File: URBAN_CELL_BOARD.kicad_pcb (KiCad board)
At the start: 2 copper layers, 162 x 181.6 mm, 20 parts, among them J1 Conn_02x09_Odd_Even, J2 Conn_01x01_Socket, J3 Conn_01x01_Socket, J4 Conn_01x01_Socket, J5 Conn_01x01_Socket

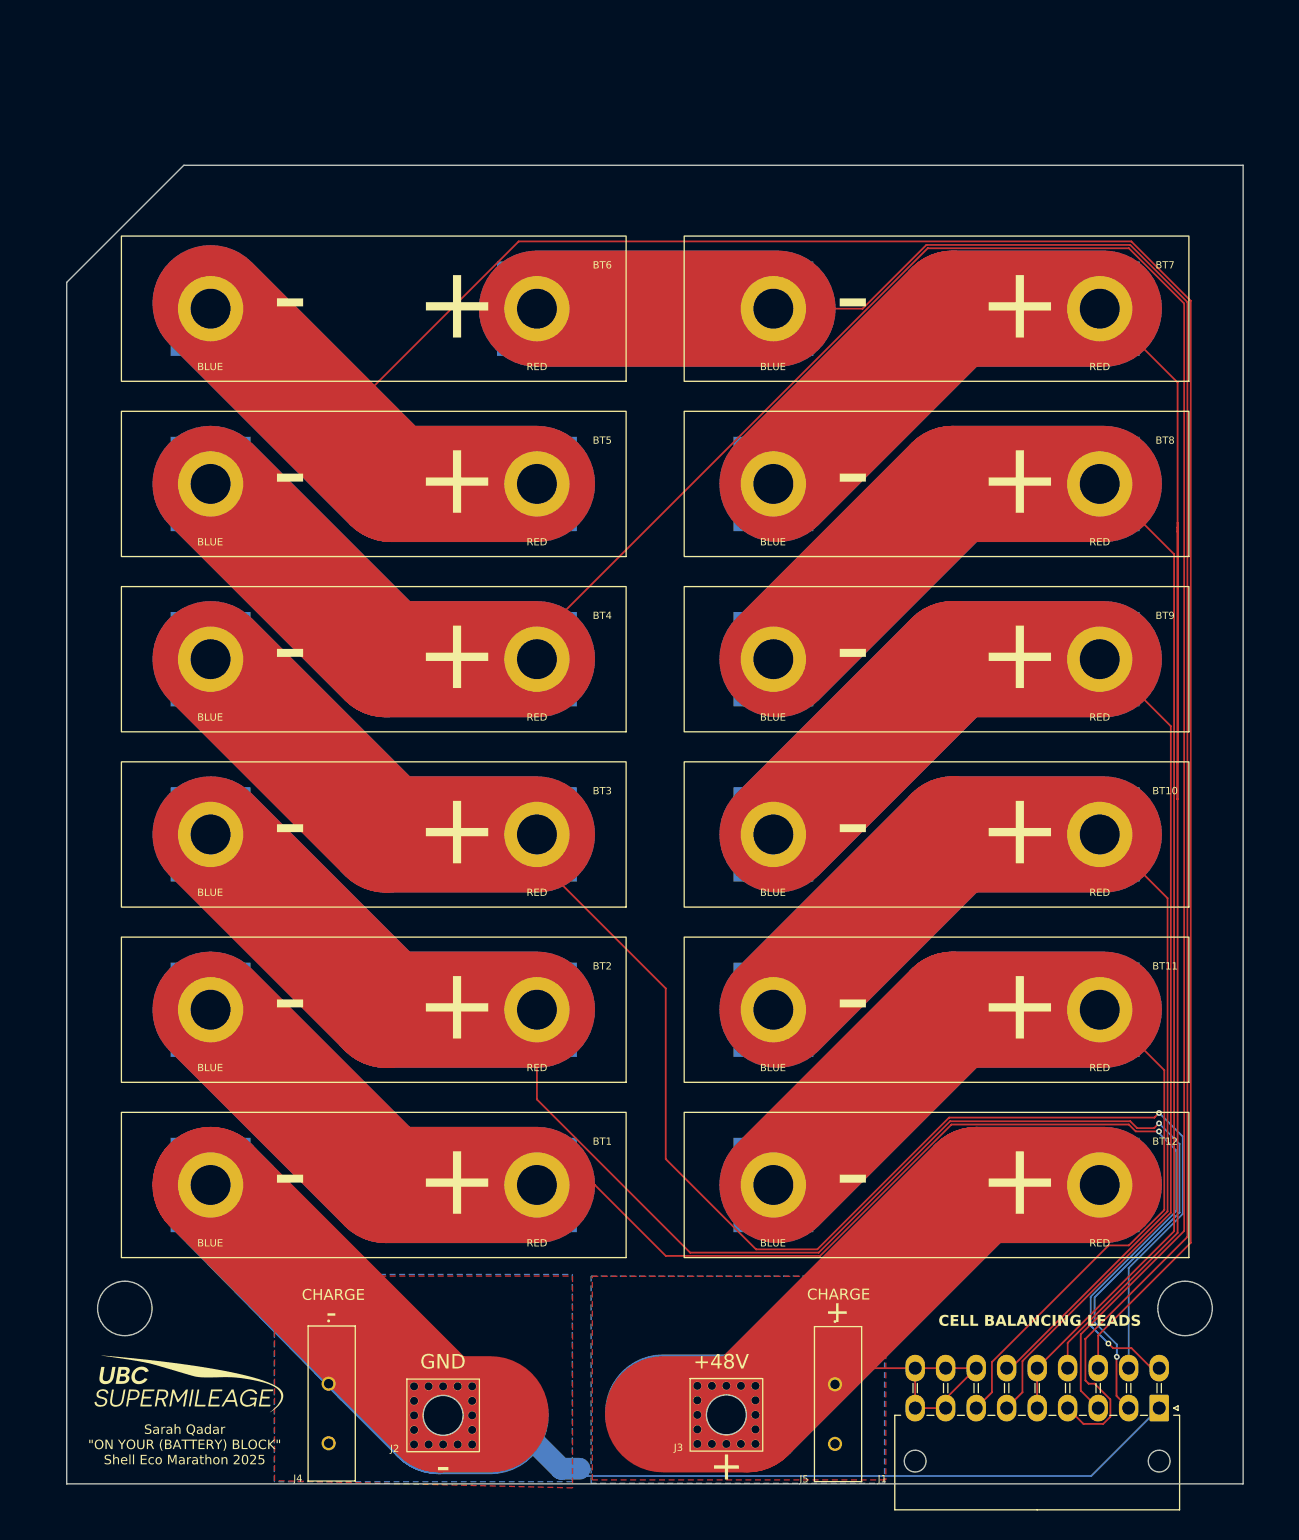
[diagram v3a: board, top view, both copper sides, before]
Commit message: new PCB layout with new cell footprint
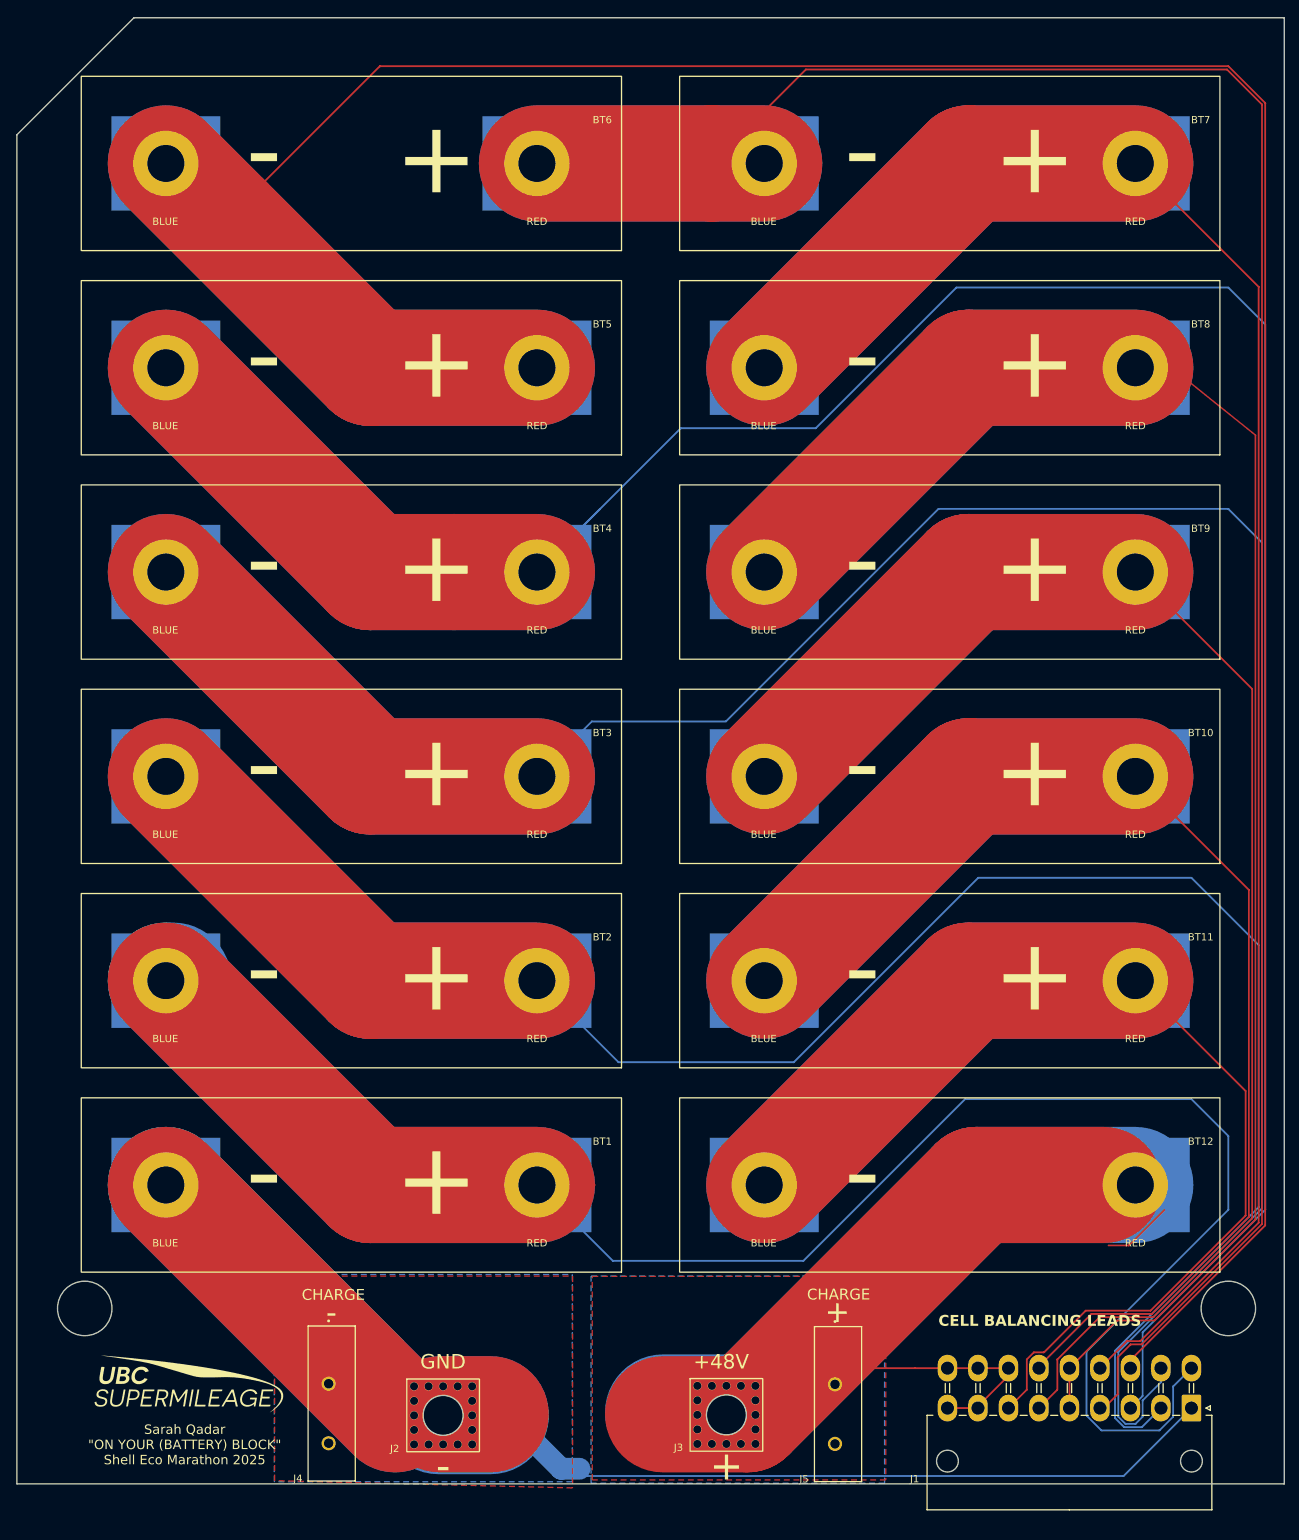
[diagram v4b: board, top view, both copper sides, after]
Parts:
- BT1, BT10, BT11, BT12, BT2, BT3, BT4, BT5, BT6, BT7, BT8, BT9: footprint Battery:Energus Li1x4pVTC6T -> URBAN_CELL_CUSTOM_footprints:Enepaq Molicel P50B 21700
- moved BT7 20.6 mm to (231.0, 99.8)
- moved BT6 20.0 mm to (148.6, 99.8)
- moved BT8 16.7 mm to (231.0, 127.9)
- moved BT5 16.0 mm to (148.6, 127.9)
- moved BT9 13.0 mm to (231.0, 156.0)
- moved BT4 12.0 mm to (148.6, 156.0)
- moved BT10 9.38 mm to (231.0, 184.2)
- moved BT3 8.00 mm to (148.6, 184.2)
- moved BT11 6.33 mm to (231.0, 212.3)
- moved H2 5.96 mm to (243.8, 257.4)
- moved H1 5.52 mm to (86.4, 257.4)
- moved BT12 4.90 mm to (231.0, 240.4)
- moved J1 4.44 mm to (238.8, 271.1)
- moved BT2 4.00 mm to (148.6, 212.3)
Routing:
- net cell3+: track 282.4 -> 391.6 mm, vias 1 -> 0
- net cell5+: track 395.1 -> 469.7 mm
- net cell1+: track 252.0 -> 314.1 mm, vias 2 -> 0
- net cell2+: track 272.0 -> 325.2 mm, vias 2 -> 0
- net GND: track 206.4 -> 259.2 mm
- net cell6+: track 298.0 -> 335.7 mm
- net cell9+: track 226.2 -> 263.8 mm
- net cell10+: track 196.5 -> 230.4 mm
- net cell4+: track 386.2 -> 418.2 mm
- net cell11+: track 180.5 -> 210.2 mm
- net cell8+: track 249.0 -> 274.5 mm
- net +48V: track 193.7 -> 208.4 mm
- net cell7+: track 305.0 -> 308.6 mm
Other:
- board size 162 x 181.6 mm -> 174.5 x 201.9 mm

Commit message: new PCB layout with new cell footprint
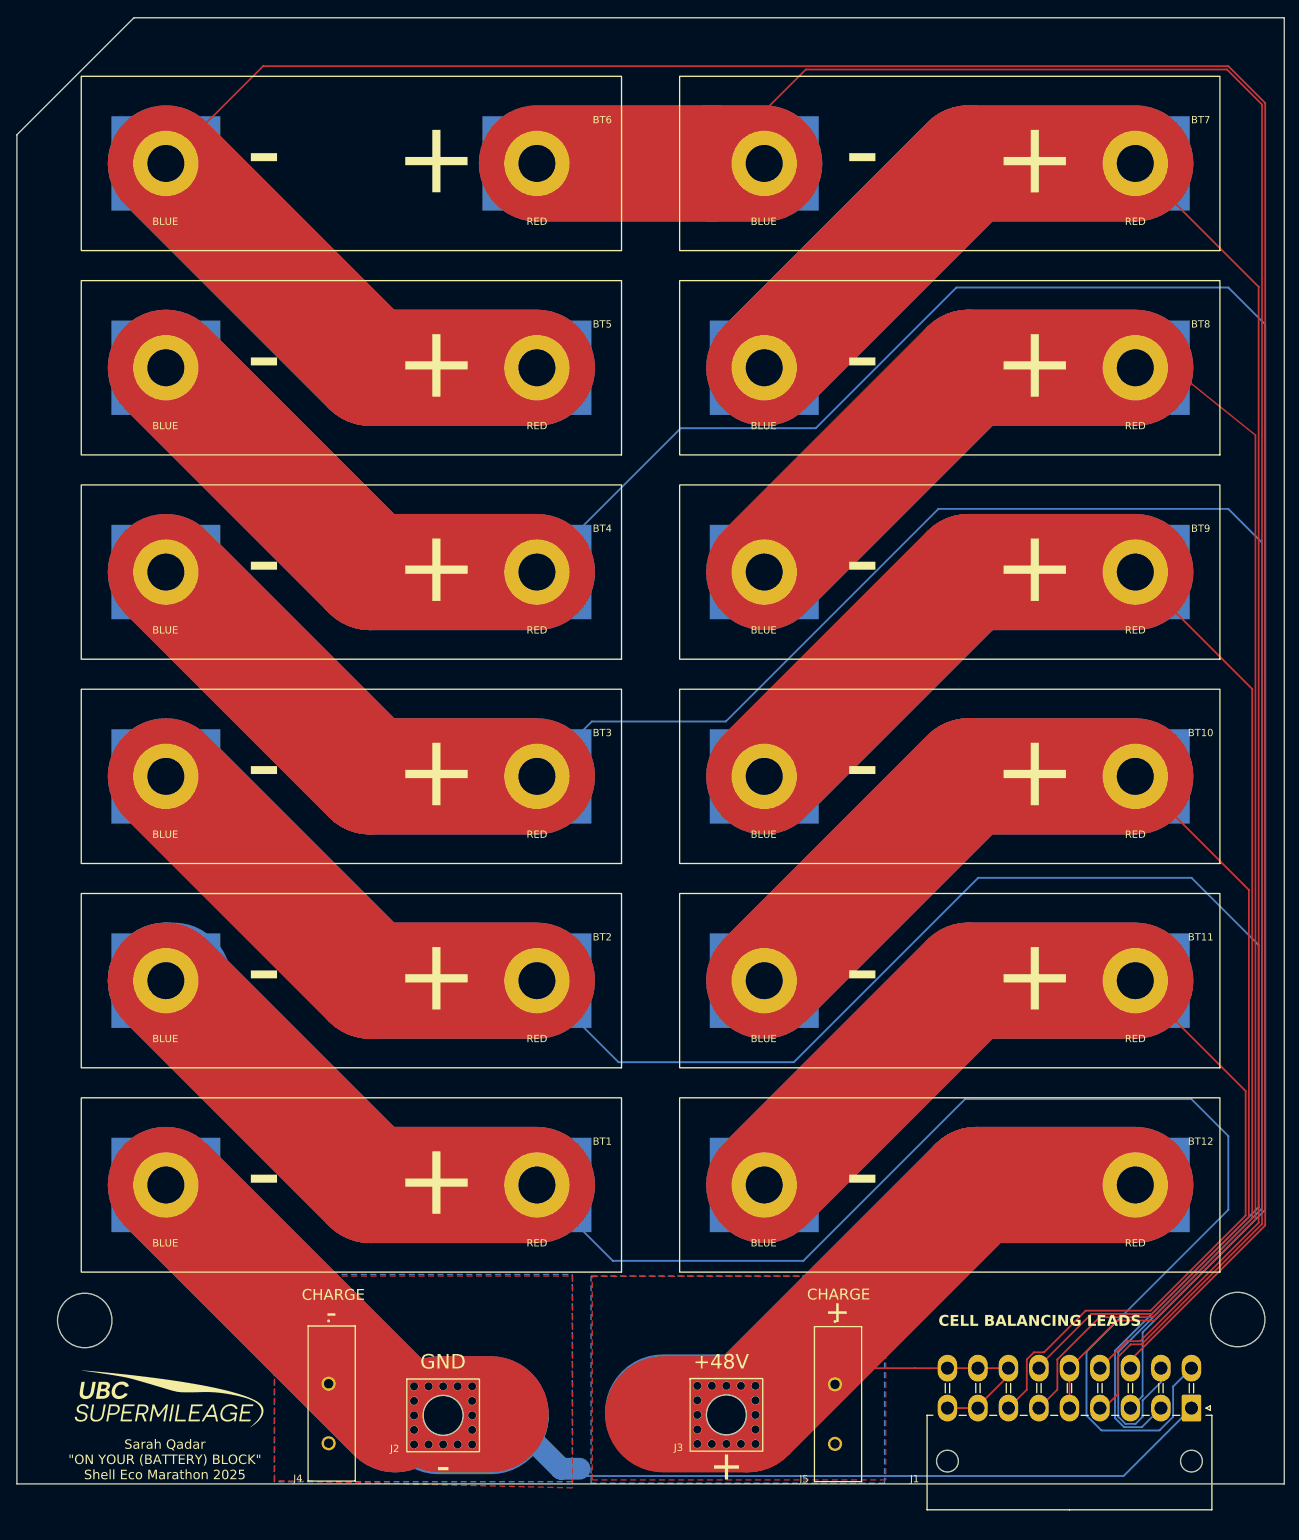
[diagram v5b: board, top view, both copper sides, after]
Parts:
- moved G*** 3.41 mm to (97.8, 270.6)
- moved H2 2.00 mm to (245.1, 259.0)
- moved H1 1.66 mm to (86.4, 259.1)
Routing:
- net GND: track 259.2 -> 221.2 mm
- net cell4+: track 418.2 -> 401.0 mm
- net cell1+: track 314.1 -> 306.1 mm
- net +48V: track 208.4 -> 203.1 mm
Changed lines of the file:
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@@
 	(footprint "LOGO"
 		(layer "F.Cu")
-		(at 100.51 268.56)
+		(at 97.788475 270.613112)
 		(property "Reference" "G***"
 			(at 0 0 0)
@@
 	(footprint "MountingHole:MountingHole_8.4mm_M8"
 		(layer "F.Cu")
-		(at 243.84 257.421)
+		(at 245.130768 258.950923)
 		(descr "Mounting Hole 8.4mm, no annular, M8")
 		(tags "mounting hole 8.4mm no annular m8")
@@
 	(footprint "MountingHole:MountingHole_8.4mm_M8"
 		(layer "F.Cu")
-		(at 86.36 257.421)
+		(at 86.36 259.08)
 		(descr "Mounting Hole 8.4mm, no annular, M8")
 		(tags "mounting hole 8.4mm no annular m8")
@@
 	)
 	(gr_text "Sarah Qadar\n{dblquote}ON YOUR (BATTERY) BLOCK{dblquote}\nShell Eco Marathon 2025"
-		(at 100.12 276.19 0)
+		(at 97.398475 278.243112 0)
 		(layer "F.SilkS")
 		(effects
@@
 	)
 	(segment
-		(start 156.601 240.421)
-		(end 148.629 240.421)
-		(width 0.25)
-		(layer "F.Cu")
-		(net 1)
-	)
-	(segment
 		(start 125.663 240.421)
 		(end 97.529 212.287)
@@
 	)
 	(segment
-		(start 97.529 240.421)
-		(end 124.359023 267.251023)
-		(width 16)
-		(layer "B.Cu")
-		(net 2)
-	)
-	(segment
 		(start 154.5 279.5)
 		(end 151.96 279.5)
@@
 	)
 	(segment
-		(start 243.84 86.36)
-		(end 127 86.36)
-		(width 0.25)
-		(layer "F.Cu")
-		(net 4)
-	)
-	(segment
 		(start 230.36 265.645)
 		(end 230.36 264.545)
@@
 	)
 	(segment
-		(start 105.569 102.711)
-		(end 105.569 107.791)
+		(start 230.36 264.545)
+		(end 248.92 245.985)
 		(width 0.25)
 		(layer "F.Cu")
@@
 	)
 	(segment
-		(start 248.92 245.985)
-		(end 248.92 243.84)
+		(start 243.84 86.36)
+		(end 110.92 86.36)
 		(width 0.25)
 		(layer "F.Cu")
@@
 	)
 	(segment
-		(start 248.92 91.44)
-		(end 243.84 86.36)
+		(start 248.92 245.985)
+		(end 248.92 91.44)
 		(width 0.25)
 		(layer "F.Cu")
@@
 	)
 	(segment
-		(start 105.569 107.791)
+		(start 110.92 86.36)
 		(end 97.529 99.751)
-		(width 16)
-		(layer "F.Cu")
-		(net 4)
-	)
-	(segment
-		(start 127 86.36)
-		(end 105.569 107.791)
 		(width 0.25)
 		(layer "F.Cu")
@@
 	)
 	(segment
-		(start 125.663 127.885)
-		(end 105.569 107.791)
-		(width 16)
-		(layer "F.Cu")
-		(net 4)
-	)
-	(segment
-		(start 230.36 264.545)
-		(end 248.92 245.985)
+		(start 248.92 91.44)
+		(end 243.84 86.36)
 		(width 0.25)
 		(layer "F.Cu")
@@
 	)
 	(segment
-		(start 248.92 243.84)
-		(end 248.92 91.44)
-		(width 0.25)
+		(start 97.529 99.751)
+		(end 125.663 127.885)
+		(width 16)
 		(layer "F.Cu")
 		(net 4)
@@
 	)
 	(segment
-		(start 137.16 156.019)
-		(end 137.16 151.127328)
-		(width 0.25)
-		(layer "F.Cu")
-		(net 5)
-	)
-	(segment
 		(start 97.529 127.885)
 		(end 125.663 156.019)
@@
 	(segment
 		(start 125.663 156.019)
-		(end 137.16 156.019)
-		(width 16)
-		(layer "F.Cu")
-		(net 5)
-	)
-	(segment
-		(start 137.16 156.019)
 		(end 148.629 156.019)
 		(width 16)
@@
 	)
 	(segment
-		(start 157.328 147.32)
-		(end 148.629 156.019)
-		(width 0.25)
-		(layer "B.Cu")
-		(net 5)
-	)
-	(segment
 		(start 206.389344 116.84)
 		(end 243.84 116.84)
@@
 	)
 	(segment
-		(start 148.629 156.019)
-		(end 168.433328 136.214672)
+		(start 168.433328 136.214672)
+		(end 148.629 156.019)
 		(width 0.25)
 		(layer "B.Cu")
@@
 	)
 	(segment
-		(start 209.159 240.421)
-		(end 226.695 240.421)
-		(width 16)
-		(layer "F.Cu")
-		(net 8)
-	)
-	(segment
 		(start 191.795 265.645)
 		(end 188 269.44)
@@
 	)
 	(segment
-		(start 230.143328 248.746)
-		(end 235.02 243.869328)
-		(width 0.25)
+		(start 209.159 240.421)
+		(end 231.029 240.421)
+		(width 16)
 		(layer "F.Cu")
 		(net 8)
@@
 		(layer "F.Cu")
 		(net 8)
-	)
-	(segment
-		(start 227.345192 248.746)
-		(end 230.143328 248.746)
-		(width 0.25)
-		(layer "F.Cu")
-		(net 8)

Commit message: updated footprint again with traces
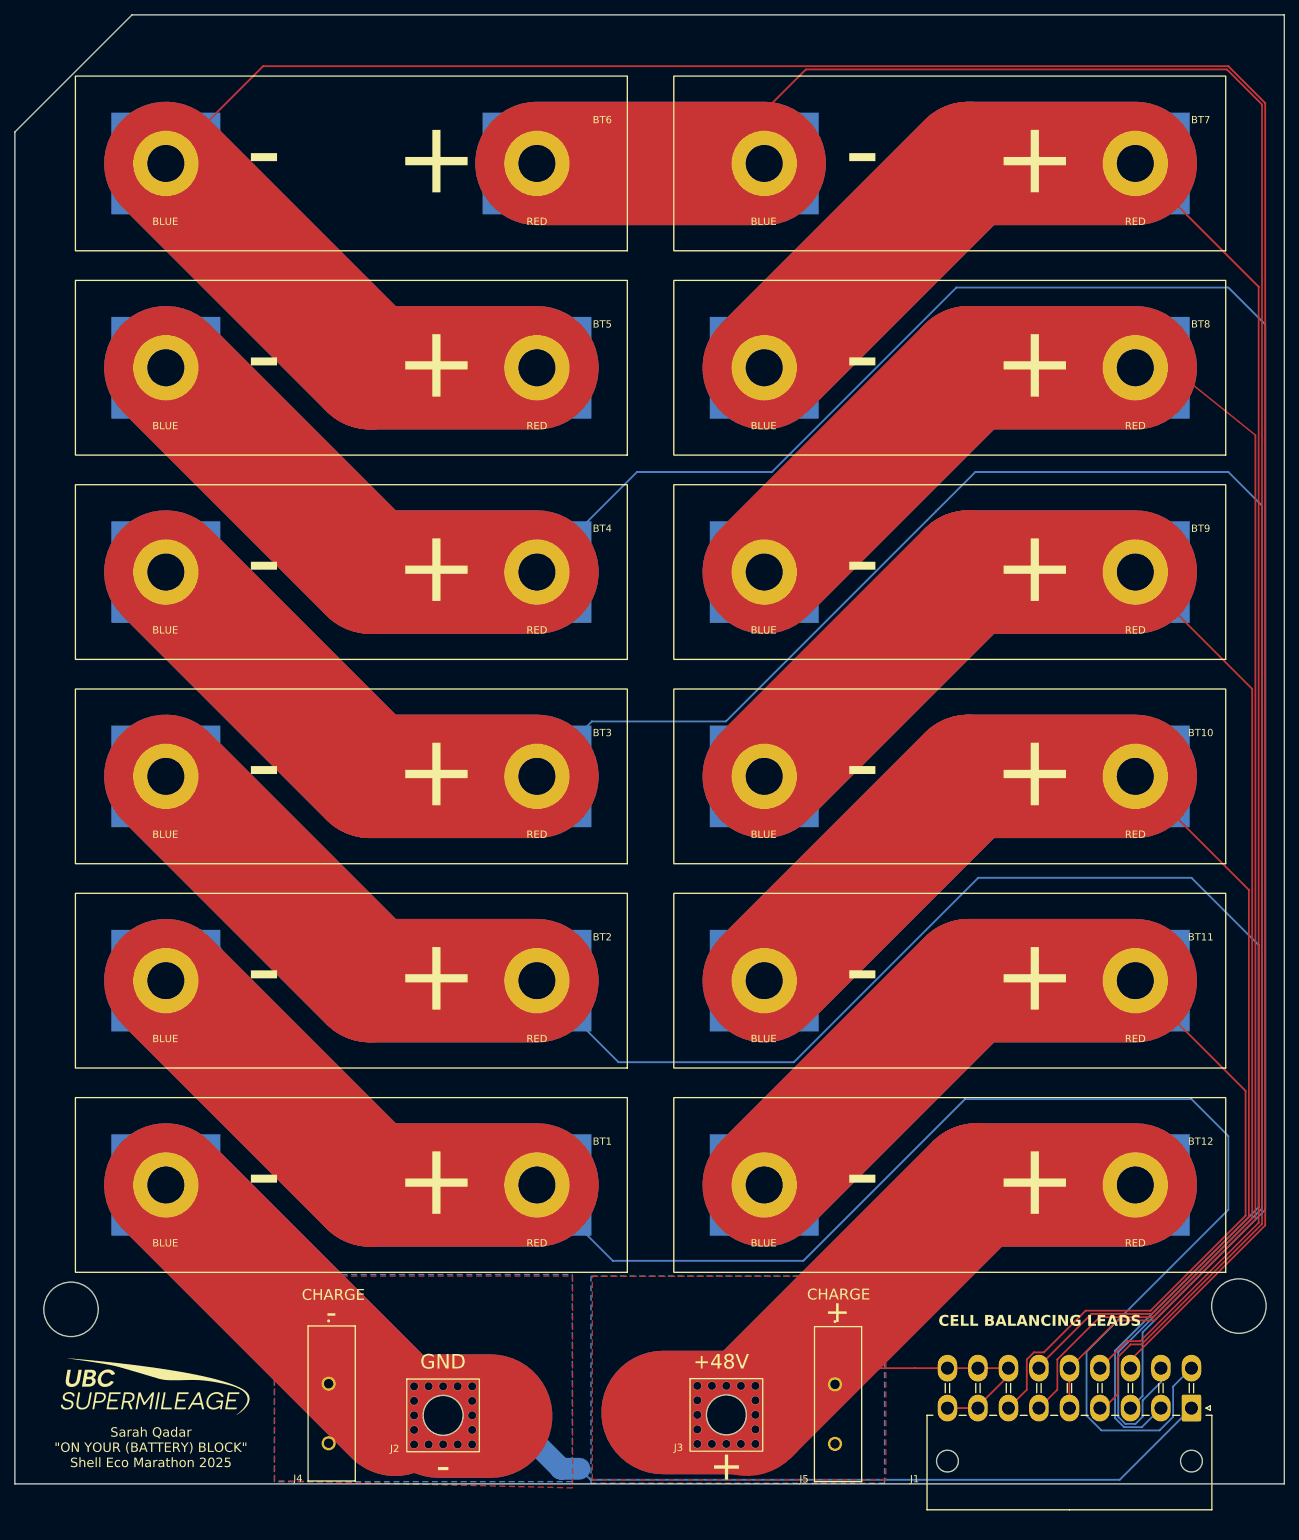
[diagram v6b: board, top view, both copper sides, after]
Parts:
- moved G*** 2.54 mm to (95.9, 268.9)
- moved H1 2.43 mm to (84.5, 257.5)
- moved H2 1.86 mm to (245.3, 257.1)
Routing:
- net cell3+: track 391.6 -> 398.8 mm
- net GND: track 221.2 -> 214.8 mm
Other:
- board size 174.5 x 201.9 mm -> 174.8 x 202.3 mm

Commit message: changed year, generated gerber and drill
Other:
- board text added: "Sarah Qadar {dblquote}ON YOUR (BATTERY) BLOCK{dblquote} Shell Eco Marathon 2026"
- board text removed: "Sarah Qadar {dblquote}ON YOUR (BATTERY) BLOCK{dblquote} Shell Eco Marathon 2025"
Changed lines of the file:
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@@
 			(usegerberextensions yes)
 			(usegerberattributes no)
-			(usegerberadvancedattributes no)
+			(usegerberadvancedattributes yes)
 			(creategerberjobfile no)
 			(dashed_line_dash_ratio 12.000000)
@@
 			(drillshape 0)
 			(scaleselection 1)
-			(outputdirectory "gerbers2.2/")
+			(outputdirectory "gerbers 2.3/")
 		)
 	)
@@
 		)
 	)
-	(gr_text "Sarah Qadar\n{dblquote}ON YOUR (BATTERY) BLOCK{dblquote}\nShell Eco Marathon 2025"
+	(gr_text "Sarah Qadar\n{dblquote}ON YOUR (BATTERY) BLOCK{dblquote}\nShell Eco Marathon 2026"
 		(at 95.476548 276.577174 0)
 		(layer "F.SilkS")
